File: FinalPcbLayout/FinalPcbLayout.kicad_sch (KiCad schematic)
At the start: 24 parts, among them J2 SPI, J4 C1, J5 Conn_02x05_Odd_Even, J6 Conn_01x02_Pin, J7 Display Socket, J8 Micro_SD_Card, J9 Conn_01x03_Pin, SW1 SW_Push, U1 ESP32-WROOM-E

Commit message: Removed Locks
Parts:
- J9: footprint Connector_PinHeader_2.54mm:PinHeader_1x03_P2.54mm_Vertical -> Connector_PinHeader_2.54mm:PinHeader_1x03_P2.54mm_Horizontal
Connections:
- net +3V3 is gone; now on net +3.3V: J9.2 (Pin_2)
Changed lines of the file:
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@@
+    )
+  )
+  (symbol (lib_id "power:+3.3V") (at 199.39 31.75 0) (unit 1)
+    (in_bom yes) (on_board yes) (dnp no) (fields_autoplaced)
+    (property "Reference" "#PWR028" (at 199.39 35.56 0)
+      (effects (font (size 1.27 1.27)) hide)
+    )
+    (property "Value" "+3.3V" (at 199.39 26.67 0)
+      (effects (font (size 1.27 1.27)))
+    )
+    (property "Footprint" "" (at 199.39 31.75 0)
+      (effects (font (size 1.27 1.27)) hide)
+    )
+    (property "Datasheet" "" (at 199.39 31.75 0)
+      (effects (font (size 1.27 1.27)) hide)
+    )
+    (pin "1")
+    (instances
+      (project "FinalPcbLayout"
+        (path "/9fcc273e-b318-4ade-b4c7-fe4ddbf9d677"
+          (reference "#PWR028") (unit 1)
+        )
+      )
     )
   )
@@
       (effects (font (size 1.27 1.27)))
     )
-    (property "Footprint" "Connector_PinHeader_2.54mm:PinHeader_1x03_P2.54mm_Vertical" (at 209.55 19.05 0)
+    (property "Footprint" "Connector_PinHeader_2.54mm:PinHeader_1x03_P2.54mm_Horizontal" (at 209.55 19.05 0)
       (effects (font (size 1.27 1.27)) hide)
     )
@@
         )
       )
-    )
-  )
-  (symbol (lib_id "power:+3V3") (at 199.39 31.75 0) (unit 1)
-    (in_bom yes) (on_board yes) (dnp no) (fields_autoplaced)
-    (property "Reference" "#PWR028" (at 199.39 35.56 0)
-      (effects (font (size 1.27 1.27)) hide)
-    )
-    (property "Value" "+3V3" (at 199.39 26.67 0)
-      (effects (font (size 1.27 1.27)))
-    )
-    (property "Footprint" "" (at 199.39 31.75 0)
-      (effects (font (size 1.27 1.27)) hide)
-    )
-    (property "Datasheet" "" (at 199.39 31.75 0)
-      (effects (font (size 1.27 1.27)) hide)
-    )
-    (pin "1")
-    (instances
-      (project "FinalPcbLayout"
-        (path "/9fcc273e-b318-4ade-b4c7-fe4ddbf9d677"
-          (reference "#PWR028") (unit 1)
-        )
-      )

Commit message: More Schematic Label Updates
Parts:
- U2: value ~ -> MAX98357
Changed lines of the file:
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@@
       (effects (font (size 1.27 1.27)))
     )
-    (property "Value" "~" (at 137.16 140.97 0)
+    (property "Value" "MAX98357" (at 137.16 140.97 0)
       (effects (font (size 1.27 1.27)))
     )

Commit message: Updated CSV
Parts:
- C12: digikey_pn (none) -> 1276-1096-6-ND
- C13: digikey_pn (none) -> 1276-1935-1-ND
- C14, C15: digikey_pn (none) -> 1276-1048-1-ND
- C25: value 22uf -> 22uF; symbol Device:C_Small -> Device:C_Polarized_Small_US; digikey_pn (none) -> 493-9831-6-ND
- C26: value 0.1uf -> 0.1uF; digikey_pn (none) -> 1276-1935-1-ND
- FB1, FB2: value FerriteBead -> 120 ohm
- J2: value SPI -> 3Term; conn_name (none) -> SPI; digikey_pn (none) -> A98334-ND
- J4: value C1 -> 3Term; conn_name (none) -> Channel 1; digikey_pn (none) -> A98334-ND
- J5: value Conn_02x05_Odd_Even -> JTAG; digikey_pn (none) -> 1175-1735-ND
- J6: value Conn_01x02_Pin -> Speaker_Out; digikey_pn (none) -> 2057-PH1RB-05-UA-ND
- J7: digikey_pn (none) -> S7012-ND
- J8: digikey_pn (none) -> WM6698CT-ND
- J9: value Conn_01x03_Pin -> Power Out
- R29: value 10k -> 10k 1%; digikey_pn (none) -> RMCF0603FT10K0CT-ND
- R8: digikey_pn (none) -> 2019-RN73H1JTTD3703F100CT-ND
- SW1: digikey_pn (none) -> A98333-ND
- U1: digikey_pn (none) -> 1965-ESP32-WROOM-32E-N8CT-ND
- U2: digikey_pn (none) -> MAX98357AETE+TCT-ND
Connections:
- net +3.3V: now also C25.1; no longer C25.2
- net GND: now also C25.2; no longer C25.1
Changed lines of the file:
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@@
       (effects (font (size 1.27 1.27)))
     )
-    (property "Value" "FerriteBead" (at 153.7208 138.43 90)
+    (property "Value" "120 ohm" (at 153.7208 138.43 90)
       (effects (font (size 1.27 1.27)))
     )
@@
       (effects (font (size 1.27 1.27)))
     )
-    (property "Value" "FerriteBead" (at 157.5308 125.73 90)
+    (property "Value" "120 ohm" (at 157.5308 125.73 90)
       (effects (font (size 1.27 1.27)))
     )
@@
   )
   (symbol (lib_id "Connector:Screw_Terminal_01x03") (at 259.08 160.02 0) (unit 1)
-    (in_bom yes) (on_board yes) (dnp no) (fields_autoplaced)
+    (in_bom yes) (on_board yes) (dnp no)
     (property "Reference" "J4" (at 261.62 158.75 0)
       (effects (font (size 1.27 1.27)) (justify left))
     )
-    (property "Value" "C1" (at 261.62 161.29 0)
+    (property "Value" "3Term" (at 261.62 161.29 0)
       (effects (font (size 1.27 1.27)) (justify left))
     )
@@
       (effects (font (size 1.27 1.27)) hide)
     )
+    (property "digikey_pn" "A98334-ND" (at 259.08 160.02 0)
+      (effects (font (size 1.27 1.27)) hide)
+    )
+    (property "conn_name" "Channel 1" (at 266.7 163.83 0)
+      (effects (font (size 1.27 1.27)))
+    )
     (pin "1")
     (pin "2")
@@
     )
     (property "Sim.Enable" "0" (at 137.16 140.97 0)
+      (effects (font (size 1.27 1.27)) hide)
+    )
+    (property "digikey_pn" "MAX98357AETE+TCT-ND" (at 137.16 140.97 0)
       (effects (font (size 1.27 1.27)) hide)
     )
@@
       (effects (font (size 1.27 1.27)))
     )
-    (property "Value" "Conn_02x05_Odd_Even" (at 254 118.11 0)
+    (property "Value" "JTAG" (at 254 118.11 0)
       (effects (font (size 1.27 1.27)))
     )
@@
     )
     (property "Sim.Enable" "0" (at 248.92 110.49 0)
+      (effects (font (size 1.27 1.27)) hide)
+    )
+    (property "digikey_pn" "1175-1735-ND" (at 248.92 110.49 0)
       (effects (font (size 1.27 1.27)) hide)
     )
@@
       (effects (font (size 1.27 1.27)))
     )
-    (property "Value" "0.1uf" (at 67.31 30.48 90)
+    (property "Value" "0.1uF" (at 67.31 30.48 90)
       (effects (font (size 1.27 1.27)))
     )
@@
       (effects (font (size 1.27 1.27)) hide)
     )
-    (property "digikey_pn" "" (at 67.31 25.4 90)
+    (property "digikey_pn" "1276-1935-1-ND" (at 67.31 25.4 90)
       (effects (font (size 1.27 1.27)) hide)
     )
@@
       (effects (font (size 1.27 1.27)) hide)
     )
+    (property "digikey_pn" "A98333-ND" (at 59.69 181.61 0)
+      (effects (font (size 1.27 1.27)) hide)
+    )
     (pin "1")
     (pin "2")
@@
     )
     (property "Sim.Enable" "0" (at 55.88 152.4 0)
+      (effects (font (size 1.27 1.27)) hide)
+    )
+    (property "digikey_pn" "WM6698CT-ND " (at 55.88 152.4 0)
       (effects (font (size 1.27 1.27)) hide)
     )
@@
       (effects (font (size 1.27 1.27)) (justify right))
     )
-    (property "Value" "Conn_01x02_Pin" (at 193.04 133.35 0)
+    (property "Value" "Speaker_Out" (at 193.04 133.35 0)
       (effects (font (size 1.27 1.27)) (justify right))
     )
@@
     )
     (property "Sim.Enable" "0" (at 191.77 133.35 0)
+      (effects (font (size 1.27 1.27)) hide)
+    )
+    (property "digikey_pn" "2057-PH1RB-05-UA-ND" (at 191.77 133.35 0)
       (effects (font (size 1.27 1.27)) hide)
     )
@@
     )
     (property "Datasheet" "https://www.espressif.com/sites/default/files/documentation/esp32-wroom-32e_esp32-wroom-32ue_datasheet_en.pdf" (at 77.47 93.98 0)
+      (effects (font (size 1.27 1.27)) hide)
+    )
+    (property "digikey_pn" "1965-ESP32-WROOM-32E-N8CT-ND" (at 77.47 55.88 0)
       (effects (font (size 1.27 1.27)) hide)
     )
@@
     )
   )
-  (symbol (lib_id "Device:C_Small") (at 67.31 21.59 90) (unit 1)
-    (in_bom yes) (on_board yes) (dnp no) (fields_autoplaced)
-    (property "Reference" "C25" (at 67.3163 15.24 90)
-      (effects (font (size 1.27 1.27)))
-    )
-    (property "Value" "22uf" (at 67.3163 17.78 90)
+  (symbol (lib_id "Device:C_Polarized_Small_US") (at 67.31 21.59 270) (mirror x) (unit 1)
+    (in_bom yes) (on_board yes) (dnp no)
+    (property "Reference" "C25" (at 67.7418 15.24 90)
+      (effects (font (size 1.27 1.27)))
+    )
+    (property "Value" "22uF" (at 67.7418 17.78 90)
       (effects (font (size 1.27 1.27)))
     )
@@
       (effects (font (size 1.27 1.27)) hide)
     )
-    (property "digikey_pn" "" (at 67.31 21.59 90)
+    (property "digikey_pn" "493-9831-6-ND" (at 67.31 21.59 90)
       (effects (font (size 1.27 1.27)) hide)
     )
@@
     )
     (property "Datasheet" "~" (at 176.53 21.59 0)
+      (effects (font (size 1.27 1.27)) hide)
+    )
+    (property "digikey_pn" "S7012-ND" (at 176.53 21.59 0)
       (effects (font (size 1.27 1.27)) hide)
     )
@@
       (effects (font (size 1.27 1.27)) hide)
     )
+    (property "digikey_pn" "1276-1048-1-ND" (at 165.1 147.32 0)
+      (effects (font (size 1.27 1.27)) hide)
+    )
     (pin "1")
     (pin "2")
@@
       (effects (font (size 1.27 1.27)) (justify left))
     )
-    (property "Value" "10k" (at 22.86 40.64 0)
+    (property "Value" "10k 1%" (at 22.86 40.64 0)
       (effects (font (size 1.27 1.27)) (justify left))
     )
@@
       (effects (font (size 1.27 1.27)) hide)
     )
+    (property "digikey_pn" "RMCF0603FT10K0CT-ND" (at 20.32 39.37 0)
+      (effects (font (size 1.27 1.27)) hide)
+    )
     (pin "1")
     (pin "2")
@@
   )
   (symbol (lib_id "Connector:Screw_Terminal_01x03") (at 252.73 137.16 0) (unit 1)
-    (in_bom yes) (on_board yes) (dnp no) (fields_autoplaced)
+    (in_bom yes) (on_board yes) (dnp no)
     (property "Reference" "J2" (at 255.27 135.89 0)
       (effects (font (size 1.27 1.27)) (justify left))
     )
-    (property "Value" "SPI" (at 255.27 138.43 0)
+    (property "Value" "3Term" (at 255.27 138.43 0)
       (effects (font (size 1.27 1.27)) (justify left))
     )
@@
     (property "Datasheet" "~" (at 252.73 137.16 0)
       (effects (font (size 1.27 1.27)) hide)
+    )
+    (property "digikey_pn" "A98334-ND" (at 252.73 137.16 0)
+      (effects (font (size 1.27 1.27)) hide)
+    )
+    (property "conn_name" "SPI" (at 256.54 140.97 0)
+      (effects (font (size 1.27 1.27)))
     )
     (pin "1")
@@
       (effects (font (size 1.27 1.27)))
     )
-    (property "Value" "Conn_01x03_Pin" (at 209.55 16.51 90)
+    (property "Value" "Power Out" (at 209.55 16.51 90)
       (effects (font (size 1.27 1.27)))
     )
@@
       (effects (font (size 1.27 1.27)) hide)
     )
+    (property "digikey_pn" "1276-1048-1-ND" (at 176.53 147.32 0)
+      (effects (font (size 1.27 1.27)) hide)
+    )
     (pin "1")
     (pin "2")
@@
       (effects (font (size 1.27 1.27)) hide)
     )
+    (property "digikey_pn" "1276-1096-6-ND" (at 104.14 156.21 0)
+      (effects (font (size 1.27 1.27)) hide)
+    )
     (pin "1")
     (pin "2")
@@
       (effects (font (size 1.27 1.27)) hide)
     )
+    (property "digikey_pn" "2019-RN73H1JTTD3703F100CT-ND" (at 110.49 125.73 0)
+      (effects (font (size 1.27 1.27)) hide)
+    )
     (pin "1")
     (pin "2")
@@
       (effects (font (size 1.27 1.27)) hide)
     )
+    (property "digikey_pn" "1276-1935-1-ND" (at 111.76 156.21 0)
+      (effects (font (size 1.27 1.27)) hide)
+    )

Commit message: Generated Bill of Materials
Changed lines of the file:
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@@
   )
   (symbol (lib_id "OSMI-parts:MAX98357") (at 137.16 140.97 0) (unit 1)
-    (in_bom yes) (on_board yes) (dnp no) (fields_autoplaced)
+    (in_bom yes) (on_board yes) (dnp no)
     (property "Reference" "U2" (at 137.16 128.27 0)
       (effects (font (size 1.27 1.27)))
     )
-    (property "Value" "MAX98357" (at 137.16 140.97 0)
+    (property "Value" "MAX98357" (at 137.16 160.02 0)
       (effects (font (size 1.27 1.27)))
     )

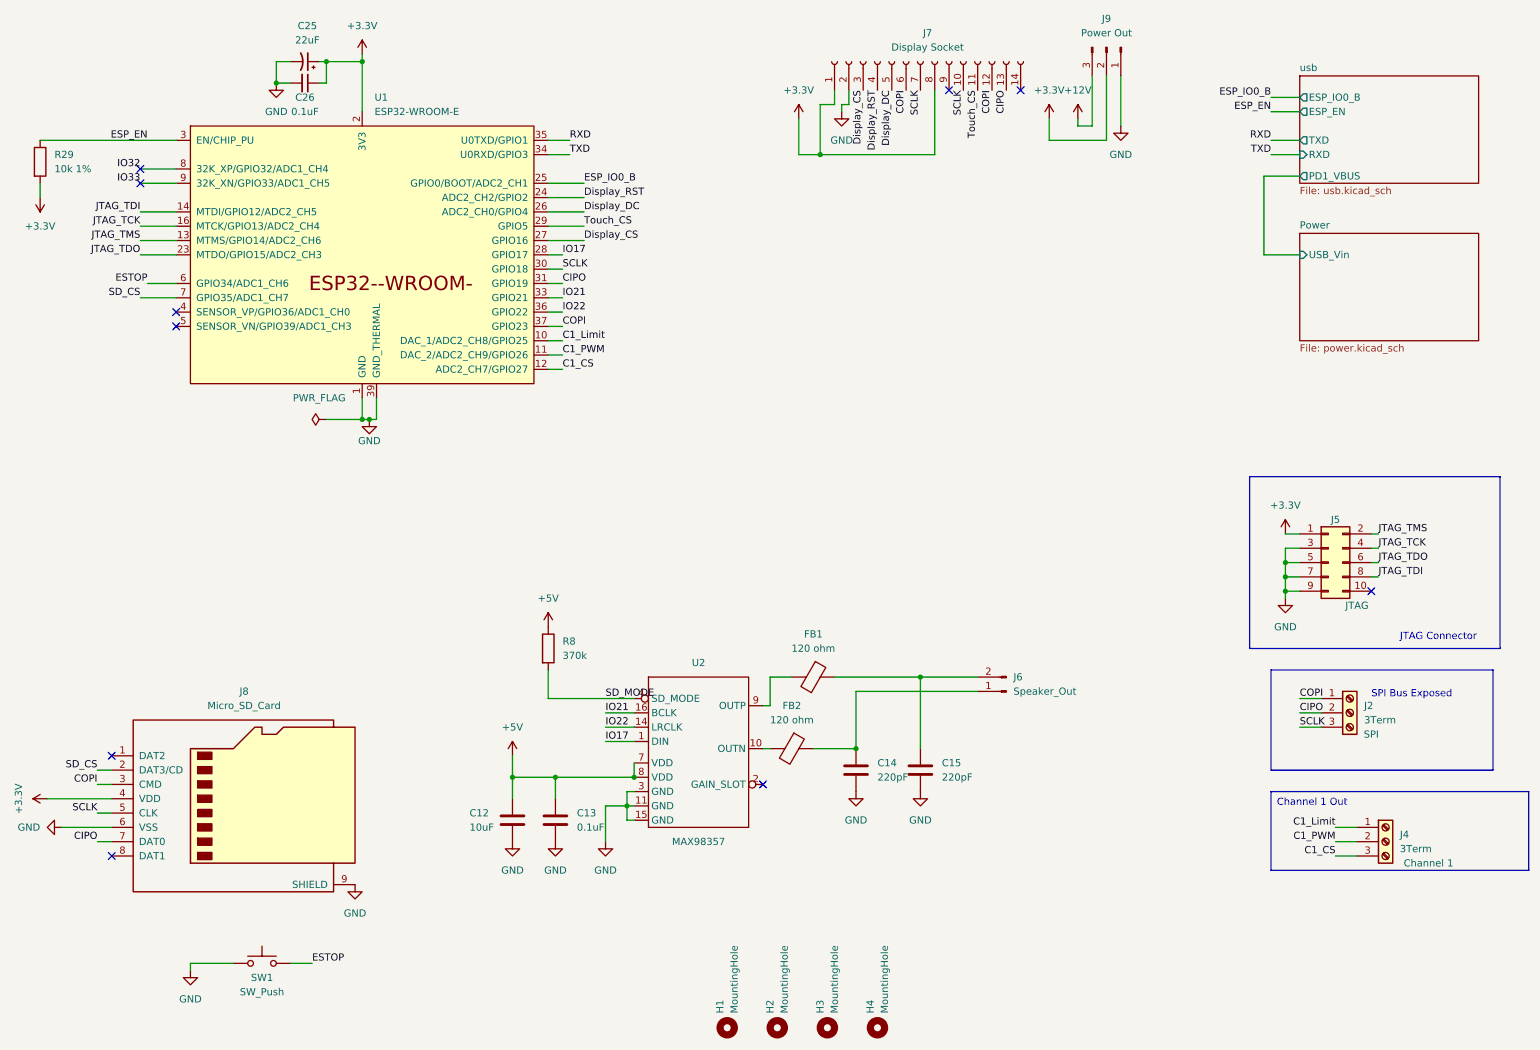
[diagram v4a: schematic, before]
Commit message: Axed Several Broken & Unused Parts
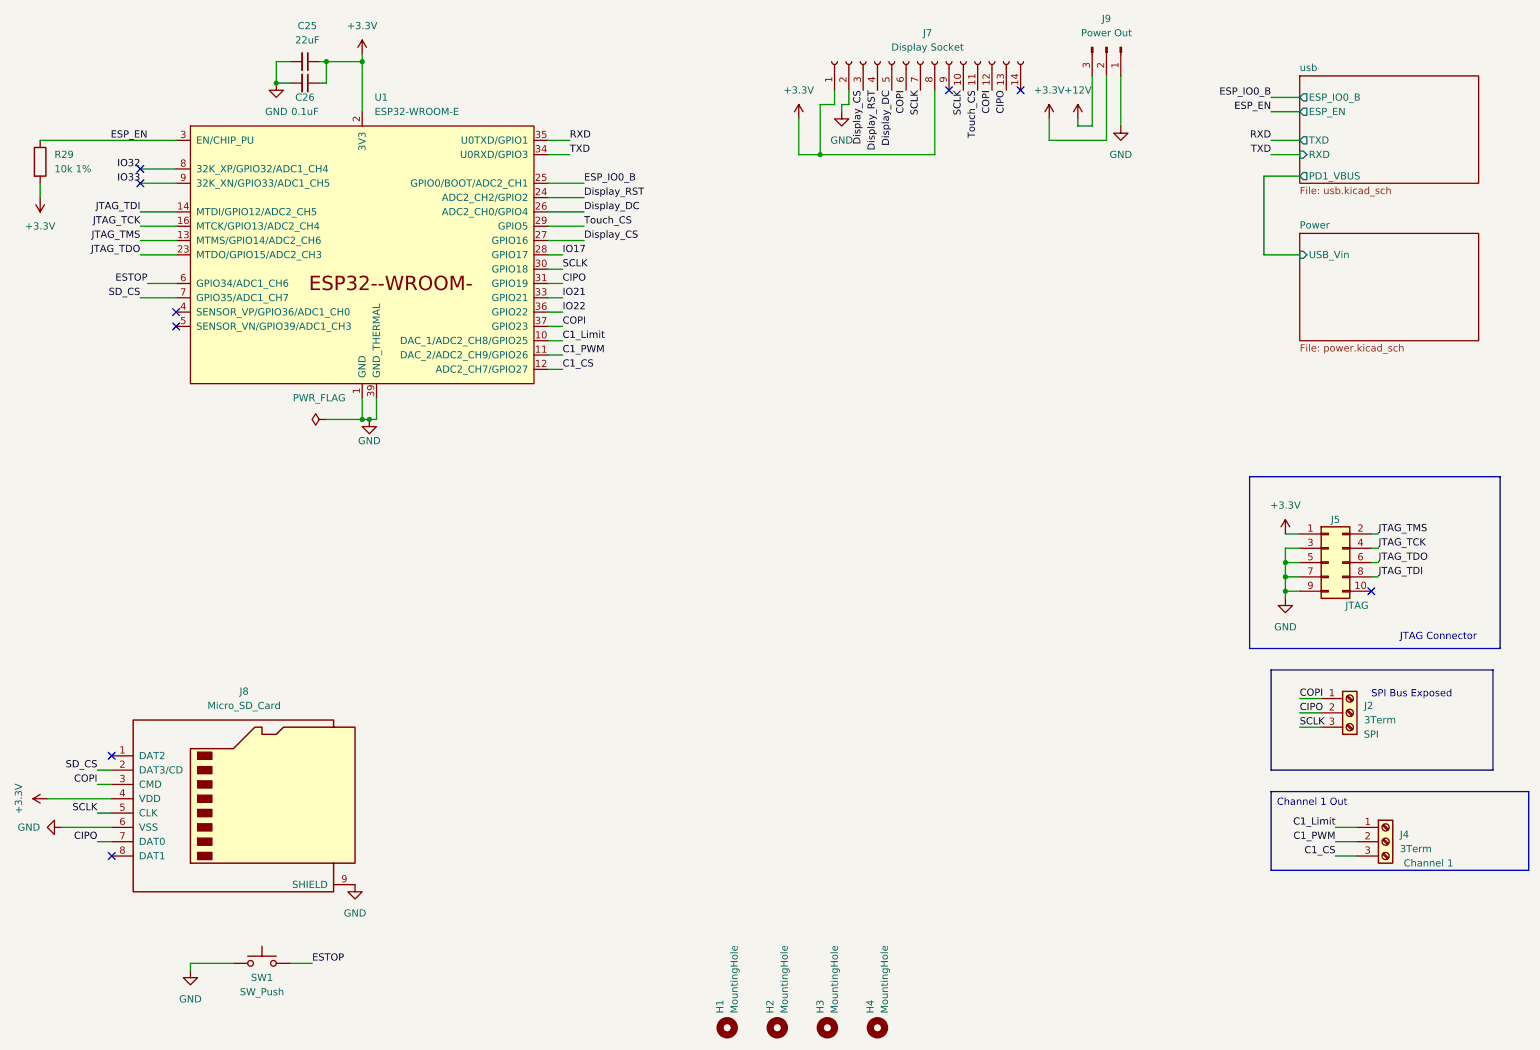
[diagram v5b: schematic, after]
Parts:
- removed C12: 10uF, Capacitor_SMD:C_0805_2012Metric, symbol Device:C
- removed C13: 0.1uF, Capacitor_SMD:C_0603_1608Metric, symbol Device:C
- removed C14, C15: 220pF, Capacitor_SMD:C_0603_1608Metric, symbol Device:C
- removed FB1, FB2: 120 ohm, Resistor_SMD:R_0603_1608Metric, symbol Device:FerriteBead
- removed J6: Speaker_Out, Connector_PinHeader_2.54mm:PinHeader_1x02_P2.54mm_Horizontal, symbol Connector:Conn_01x02_Pin
- removed R8: 370k, Resistor_SMD:R_0603_1608Metric, symbol Device:R
- removed U2: MAX98357, Package_DFN_QFN:QFN-16-1EP_3x3mm_P0.5mm_EP1.45x1.45mm, symbol OSMI-parts:MAX98357
- C25: symbol Device:C_Polarized_Small_US -> Device:C_Small; Notes (none) -> Class 2 Dielectric; digikey_pn 493-9831-6-ND -> (none)
- C26: Notes (none) -> Class 2 Dielectric
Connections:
- no-connect marks 10 -> 9

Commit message: Working on USB to UART
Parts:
- removed C25: 22uF, Capacitor_SMD:C_Elec_4x5.4, symbol Device:C_Small
- removed J2, J4: 3Term, TerminalBlock_TE-Connectivity:TerminalBlock_TE_282834-3_1x03_P2.54mm_Horizontal, symbol Connector:Screw_Terminal_01x03
- removed J9: Power Out, Connector_PinHeader_2.54mm:PinHeader_1x03_P2.54mm_Horizontal, symbol Connector:Conn_01x03_Pin
- removed SW1: SW_Push, TerminalBlock_TE-Connectivity:TerminalBlock_TE_282834-2_1x02_P2.54mm_Horizontal, symbol Switch:SW_Push
- added J2: Conn_02x06_Counter_Clockwise, symbol Connector_Generic:Conn_02x06_Counter_Clockwise
- J7: footprint Connector_PinSocket_2.54mm:PinSocket_1x14_P2.54mm_Vertical -> Connector_PinSocket_2.54mm:PinSocket_1x14_P2.54mm_Vertical_SMD_Pin1Left
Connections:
- net IO33 is gone; now on net SD_CS: U1.9 (32K_XN/GPIO33/ADC1_CH5)
- net +12V: now also J2.1 (Pin_1)
- net C1_CS: now also J2.5 (Pin_5)
- net C1_Limit: now also J2.11 (Pin_11)
- net C1_PWM: now also J2.10 (Pin_10)
- net CIPO: now also J2.3 (Pin_3)
- net COPI: now also J2.2 (Pin_2)
- net GND: now also J2.6 (Pin_6), J2.7 (Pin_7)
- net SCLK: now also J2.4 (Pin_4)
- net SD_CS: no longer U1.7 (GPIO35/ADC1_CH7)
- net IO17 renamed C1_ENC_P
- net C1_ENC_P: now also J2.9 (Pin_9)
- net IO21 renamed C1_ENC_N
- net C1_ENC_N: now also J2.8 (Pin_8)
- net IO22: no longer names the net of U1.36 (GPIO22)
- net IO32: no longer names the net of U1.8 (32K_XP/GPIO32/ADC1_CH4)
- new net +3V3: J2.12 (Pin_12)
- no-connect marks 9 -> 10
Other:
- note removed: "SPI Bus Exposed"
- moved on the sheet: C26, J5

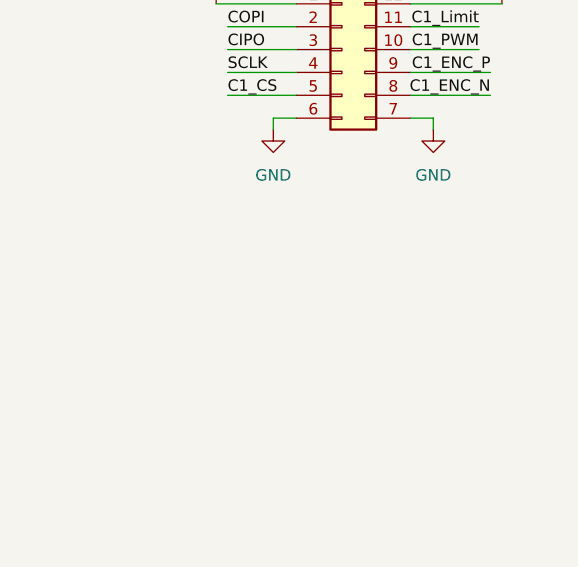
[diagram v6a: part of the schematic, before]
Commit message: adv channel control
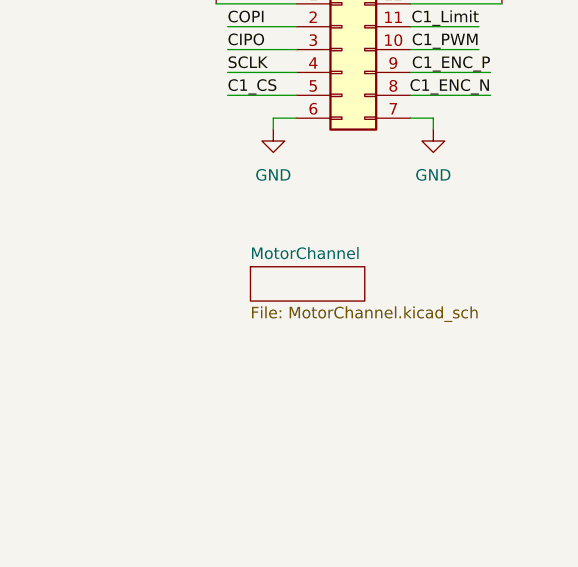
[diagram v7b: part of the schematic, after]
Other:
- added sheet MotorChannel (MotorChannel.kicad_sch)
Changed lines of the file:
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@@
+	)
+	(sheet
+		(at 246.38 149.86)
+		(size 12.7 3.81)
+		(fields_autoplaced yes)
+		(stroke
+			(width 0.1524)
+			(type solid)
+		)
+		(fill
+			(color 0 0 0 0.0000)
+		)
+		(property "Sheetname" "MotorChannel"
+			(at 246.38 149.1484 0)
+			(effects
+				(font
+					(size 1.27 1.27)
+				)
+				(justify left bottom)
+			)
+		)
+		(property "Sheetfile" "MotorChannel.kicad_sch"
+			(at 246.38 154.2546 0)
+			(effects
+				(font
+					(size 1.27 1.27)
+				)
+				(justify left top)
+			)
+		)
+		(instances
+			(project "FinalPcbLayout"
+				(path "/9fcc273e-b318-4ade-b4c7-fe4ddbf9d677"
+					(page "4")
+				)
+			)
+		)
 	)
 	(sheet
